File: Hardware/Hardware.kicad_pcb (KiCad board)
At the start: 2 copper layers, 108 x 60 mm, 65 parts, among them J1 LINEIN, J2 MICIN, J3 Raspberry_Pi_2_3, J4 LOUT, J5 HPOUT, SW1 JS5208, U1 MCP3004, U2 WM8731SEDS

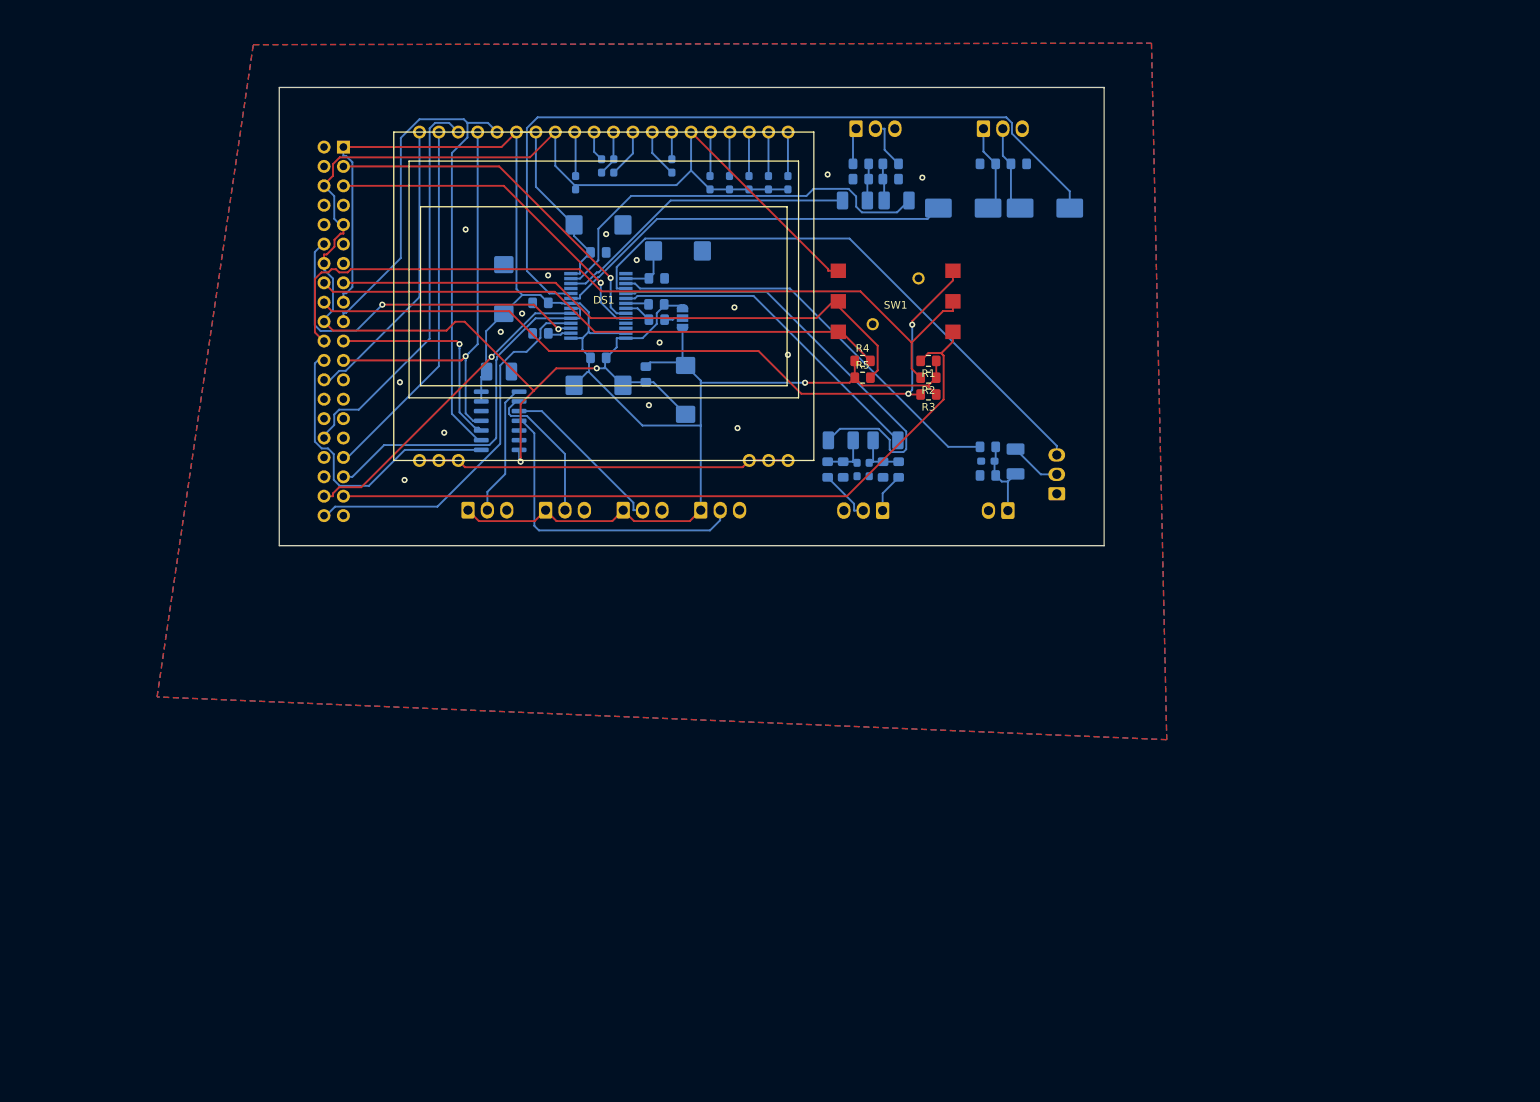
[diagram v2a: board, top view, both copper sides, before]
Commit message: Cleaned up traces, organised silkscreen, stitched ground planes.
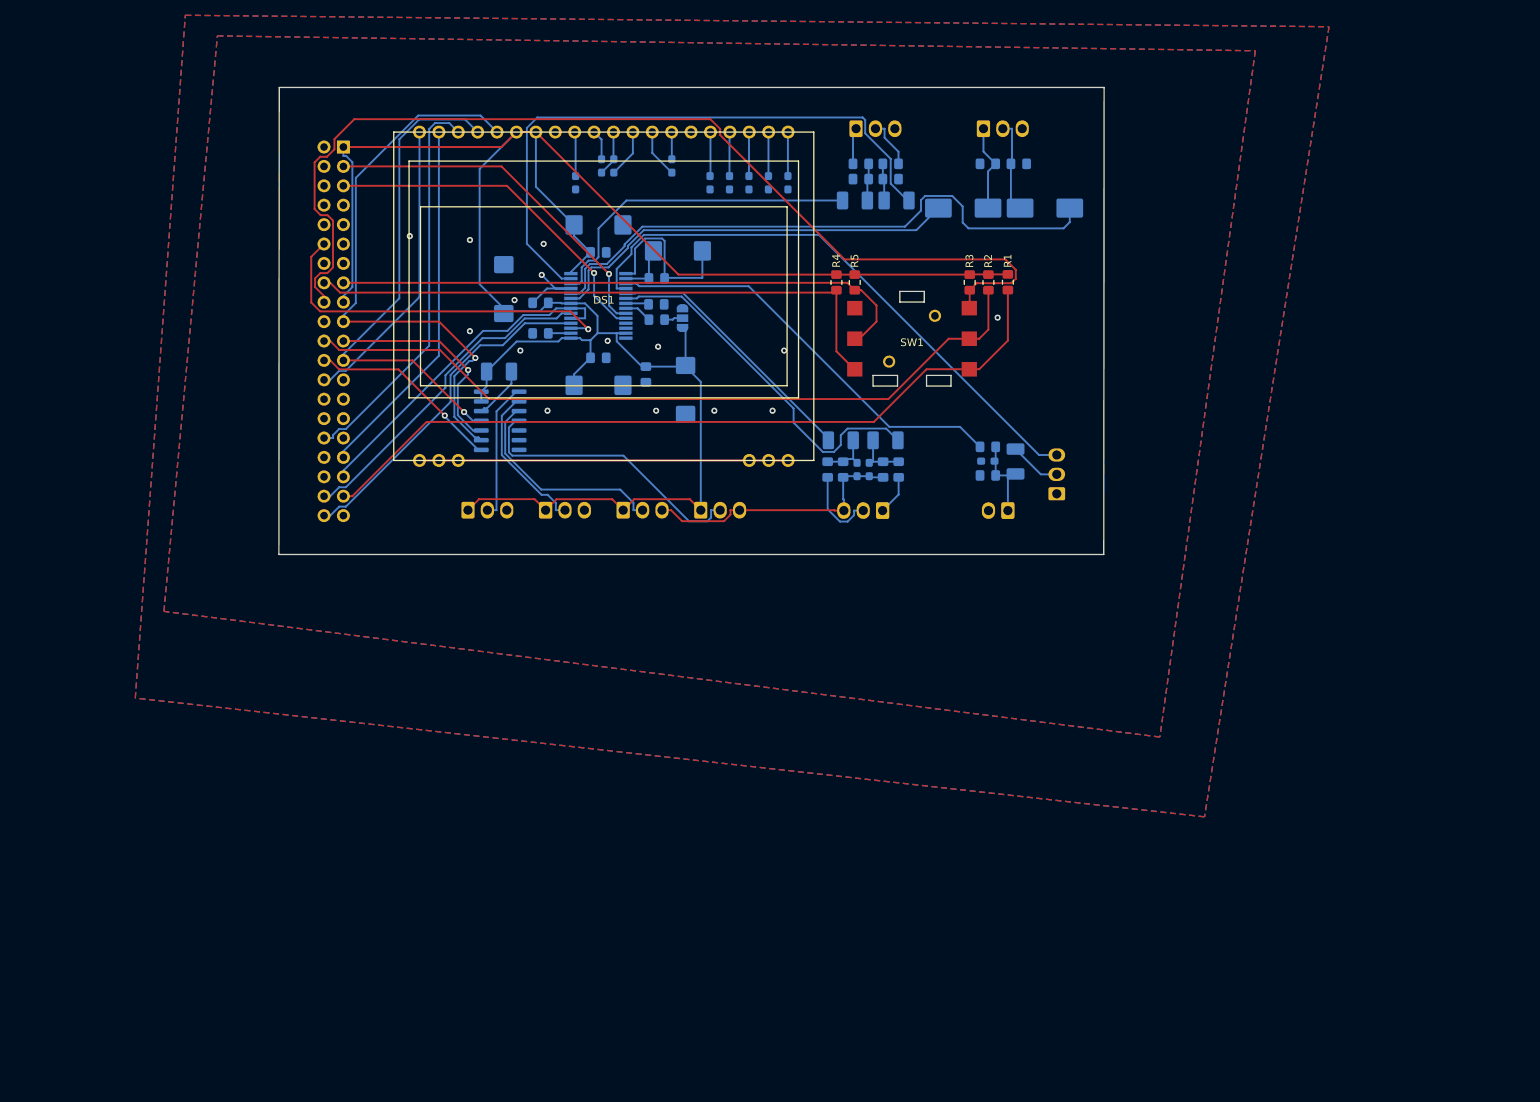
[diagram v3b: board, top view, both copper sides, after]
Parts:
- added G***: LOGO, signl:signl_logo, B.Cu at (164.8, 55.4)
- moved R3 15.6 mm to (158.4, 51.5), turned to 270 degrees
- moved R2 14.7 mm to (160.8, 51.5), turned to 270 degrees
- moved R1 14.6 mm to (163.4, 51.5), turned to 270 degrees
- moved R5 12.5 mm to (143.3, 51.5), turned to 270 degrees
- moved R4 10.8 mm to (140.9, 51.5), turned to 270 degrees
- moved SW1 5.35 mm to (150.8, 58.9)
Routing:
- net GNDD: track 209.8 -> 0.00 mm, vias 2 -> 12
- net GNDA: track 0.00 -> 74.9 mm, vias 16 -> 3
- net /CTRLUP: track 101.7 -> 135.6 mm, vias 2 -> 0
- net +3V3: track 255.7 -> 284.2 mm, vias 1 -> 0
- net /ROUT: track 54.3 -> 80.8 mm
- net /RHPOUT: track 104.4 -> 78.2 mm
- net /RLINEIN: track 59.7 -> 34.7 mm
- net /~CS~: track 39.7 -> 25.5 mm, vias 0 -> 1
- net /DISP_MOSI: track 85.9 -> 75.4 mm, vias 0 -> 1
- net /DISP_SCK: track 56.2 -> 65.3 mm
- net /CTRLRIGHT: track 105.1 -> 99.1 mm
- net /CTRLC: track 22.1 -> 28.2 mm
- net /CTRLDOWN: track 96.6 -> 102.1 mm
- net /DACDAT: track 49.4 -> 44.8 mm
- net /LLINEIN: track 43.6 -> 47.9 mm
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- added copper zone on B.Cu, net GNDD
- added copper zone on F.Cu, net GNDD
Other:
- board size 108 x 60 mm -> 108 x 61.2 mm
- board text added: "Rev 1. Alexander Strachan Robert Norris Simon Ridley"
